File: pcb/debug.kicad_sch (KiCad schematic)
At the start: 2 parts

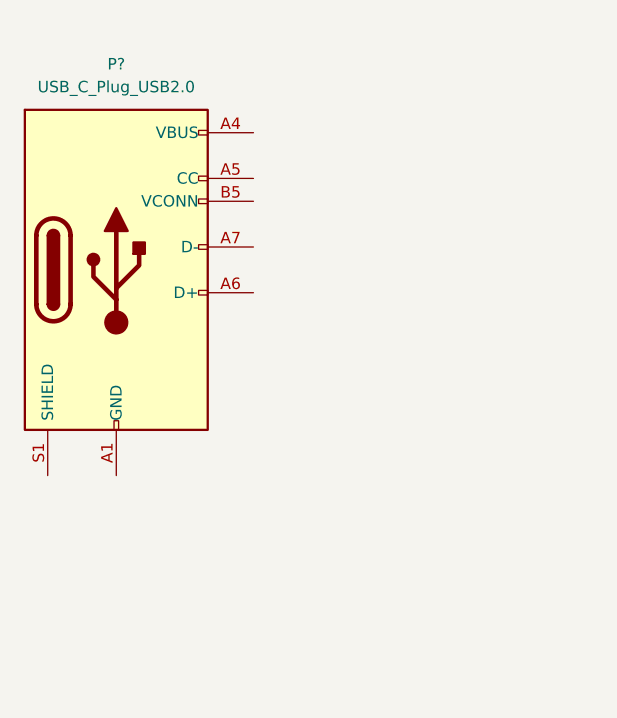
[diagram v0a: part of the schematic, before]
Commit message: add power schematics
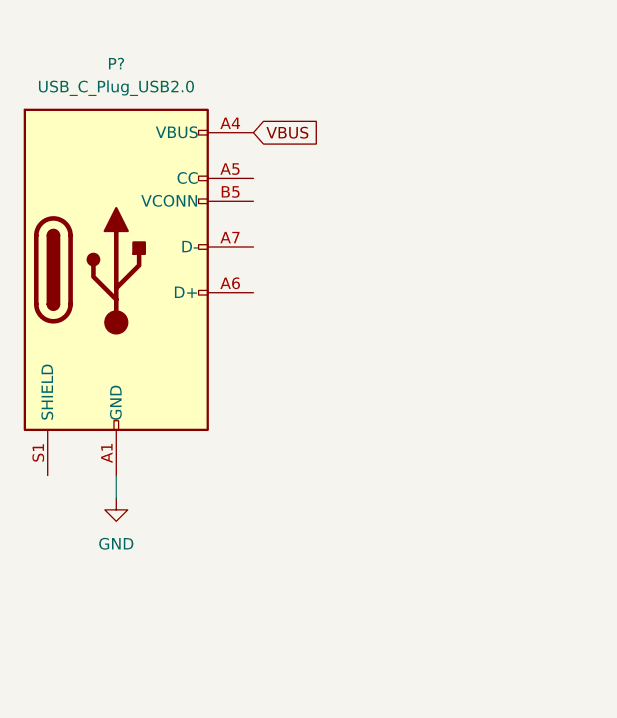
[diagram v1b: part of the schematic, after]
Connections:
- net GND: now reaches P?.A1 (GND), P?.A12 (GND), P?.B1 (GND), P?.B12 (GND)
- net VBUS: now reaches P?.A4 (VBUS), P?.A9 (VBUS), P?.B4 (VBUS), P?.B9 (VBUS)
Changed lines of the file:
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@@
     (title "USB to SPI interface")
+  )
+  (wire (pts (xy 45.72 115.57) (xy 45.72 118.11))
+    (stroke (width 0) (type default) (color 0 0 0 0))
+  )
+  (global_label "VBUS" (shape input) (at 60.96 77.47 0) (fields_autoplaced)
+    (effects (font (size 1.27 1.27)) (justify left))
+    (property "Intersheet References" "${INTERSHEET_REFS}" (id 0) (at 68.2717 77.3906 0)
+      (effects (font (size 1.27 1.27)) (justify left))
+    )
   )
   (symbol (lib_id "Connector:USB_C_Plug_USB2.0") (at 45.72 92.71 0) (unit 1)
@@
     (pin "9")
   )
+  (symbol (lib_id "power:GND") (at 45.72 118.11 0) (unit 1)
+    (in_bom yes) (on_board yes) (fields_autoplaced)
+    (property "Reference" "#PWR?" (id 0) (at 45.72 124.46 0)
+      (effects (font (size 1.27 1.27)) hide)
+    )
+    (property "Value" "GND" (id 1) (at 45.72 123.19 0))
+    (property "Footprint" "" (id 2) (at 45.72 118.11 0)
+      (effects (font (size 1.27 1.27)) hide)
+    )
+    (property "Datasheet" "" (id 3) (at 45.72 118.11 0)
+      (effects (font (size 1.27 1.27)) hide)
+    )
+    (pin "1")
+  )
   (sheet (at 171.45 219.71) (size 24.13 19.05) (fields_autoplaced)
     (stroke (width 0.1524) (type solid) (color 0 0 0 0))
@@
   )
   (symbol_instances
+    (path "/1b1ae3dd-f20e-4dc4-843b-d424ca135075/2e74d807-b0fe-4e20-9ef7-ed84c7863992"
+      (reference "#FLG?") (unit 1) (value "PWR_FLAG") (footprint "")
+    )
+    (path "/1b1ae3dd-f20e-4dc4-843b-d424ca135075/2d21afbd-6859-4669-a772-031efa34f4ca"
+      (reference "#PWR?") (unit 1) (value "+3V3") (footprint "")
+    )
+    (path "/1b1ae3dd-f20e-4dc4-843b-d424ca135075/45f16f4e-0be6-4730-a0ff-76769f804a66"
+      (reference "#PWR?") (unit 1) (value "+5V") (footprint "")
+    )
+    (path "/dfea10a7-1cbe-4c44-a951-08c8c82414b9/50fb4ca1-22a3-4466-ab42-e0b30b8cb45f"
+      (reference "#PWR?") (unit 1) (value "GND") (footprint "")
+    )
+    (path "/dfea10a7-1cbe-4c44-a951-08c8c82414b9/58475425-b42f-4af3-9c27-3bfb381b9dbc"
+      (reference "#PWR?") (unit 1) (value "GND") (footprint "")
+    )
+    (path "/94884f5c-d59b-4b75-abd7-44726b7a235a"
+      (reference "#PWR?") (unit 1) (value "GND") (footprint "")
+    )
+    (path "/1b1ae3dd-f20e-4dc4-843b-d424ca135075/a43f493d-f709-4ca9-9df9-a46685d2f7a2"
+      (reference "#PWR?") (unit 1) (value "GND") (footprint "")
+    )
+    (path "/1b1ae3dd-f20e-4dc4-843b-d424ca135075/bc7f0831-fb41-4e41-b4a1-87de6e384650"
+      (reference "#PWR?") (unit 1) (value "GND") (footprint "")
+    )
+    (path "/1b1ae3dd-f20e-4dc4-843b-d424ca135075/ca0117f5-c935-4a15-9120-d20f94ec645f"
+      (reference "#PWR?") (unit 1) (value "GND") (footprint "")
+    )
+    (path "/1b1ae3dd-f20e-4dc4-843b-d424ca135075/e18d338e-e566-43ef-ab1a-e91845ba4607"
+      (reference "#PWR?") (unit 1) (value "+5V") (footprint "")
+    )
+    (path "/dfea10a7-1cbe-4c44-a951-08c8c82414b9/f0208d8e-9c49-4e8a-9555-afee527cca7a"
+      (reference "#PWR?") (unit 1) (value "GND") (footprint "")
+    )
+    (path "/1b1ae3dd-f20e-4dc4-843b-d424ca135075/f0f17df2-bb70-4da8-ab70-70dc33265364"
+      (reference "#PWR?") (unit 1) (value "GND") (footprint "")
+    )
+    (path "/1b1ae3dd-f20e-4dc4-843b-d424ca135075/f5b12451-8c10-452e-97b4-d0279ae5f0a0"
+      (reference "#PWR?") (unit 1) (value "+5V") (footprint "")
+    )
+    (path "/1b1ae3dd-f20e-4dc4-843b-d424ca135075/9e702b4b-af83-4225-99e7-d3b37033d4f6"
+      (reference "C?") (unit 1) (value "1u") (footprint "")
+    )
+    (path "/1b1ae3dd-f20e-4dc4-843b-d424ca135075/d31985b9-4de6-488d-a2f4-75966192efdf"
+      (reference "C?") (unit 1) (value "1u") (footprint "")
+    )
+    (path "/1b1ae3dd-f20e-4dc4-843b-d424ca135075/fcdaf3af-f4d4-427c-8c20-ed0729a5b02a"
+      (reference "C?") (unit 1) (value "1u") (footprint "")
+    )
+    (path "/1b1ae3dd-f20e-4dc4-843b-d424ca135075/3f6b5f2a-45d9-4080-aba4-0ff576a8a80f"
+      (reference "FB?") (unit 1) (value "600R") (footprint "")
+    )
     (path "/dfea10a7-1cbe-4c44-a951-08c8c82414b9/4ec00cc8-73ee-4a88-8f61-16dd24bb6fe7"
       (reference "J?") (unit 1) (value "09031966921") (footprint "Harting-09031966921-0-0-*")
@@
       (reference "P?") (unit 1) (value "USB_C_Plug_USB2.0") (footprint "")
     )
-    (path "/1b1ae3dd-f20e-4dc4-843b-d424ca135075/64f3e14b-8a0a-445b-842d-7829e058b95b"
-      (reference "Q?") (unit 1) (value "Q_NPN_BCE") (footprint "")
+    (path "/1b1ae3dd-f20e-4dc4-843b-d424ca135075/f8a17ca4-324e-4b9e-940d-3e3a6aba4552"
+      (reference "Q?") (unit 1) (value "Q_PNP_BCE") (footprint "")
+    )
+    (path "/1b1ae3dd-f20e-4dc4-843b-d424ca135075/e6d3f2ec-0651-4501-9d4b-6ed215e299b7"
+      (reference "R?") (unit 1) (value "R_Small") (footprint "")
     )
     (path "/22bb6c80-05a9-4d89-98b0-f4c23fe6c1ce"

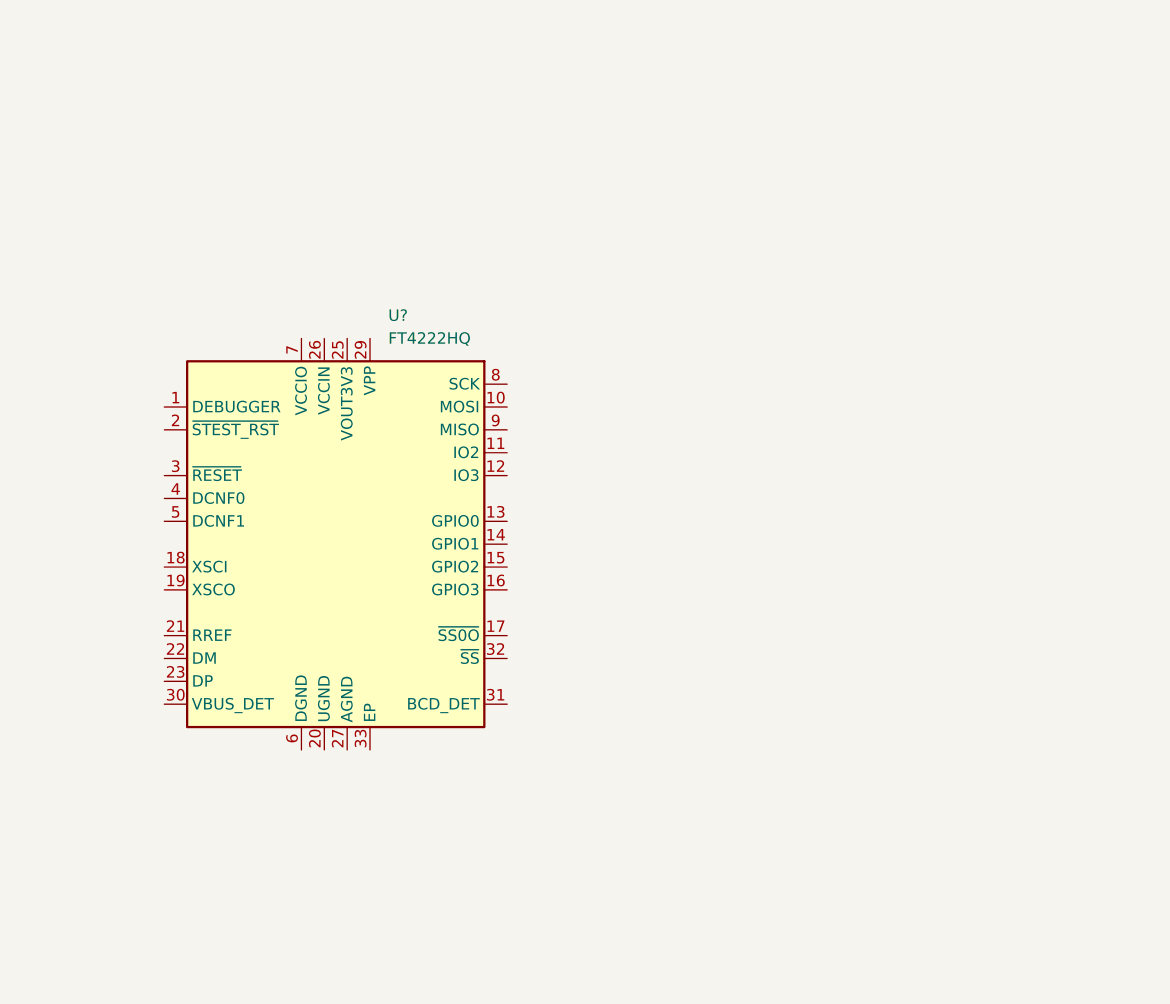
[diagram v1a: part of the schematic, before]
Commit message: start the schematics for the usb to spi interface
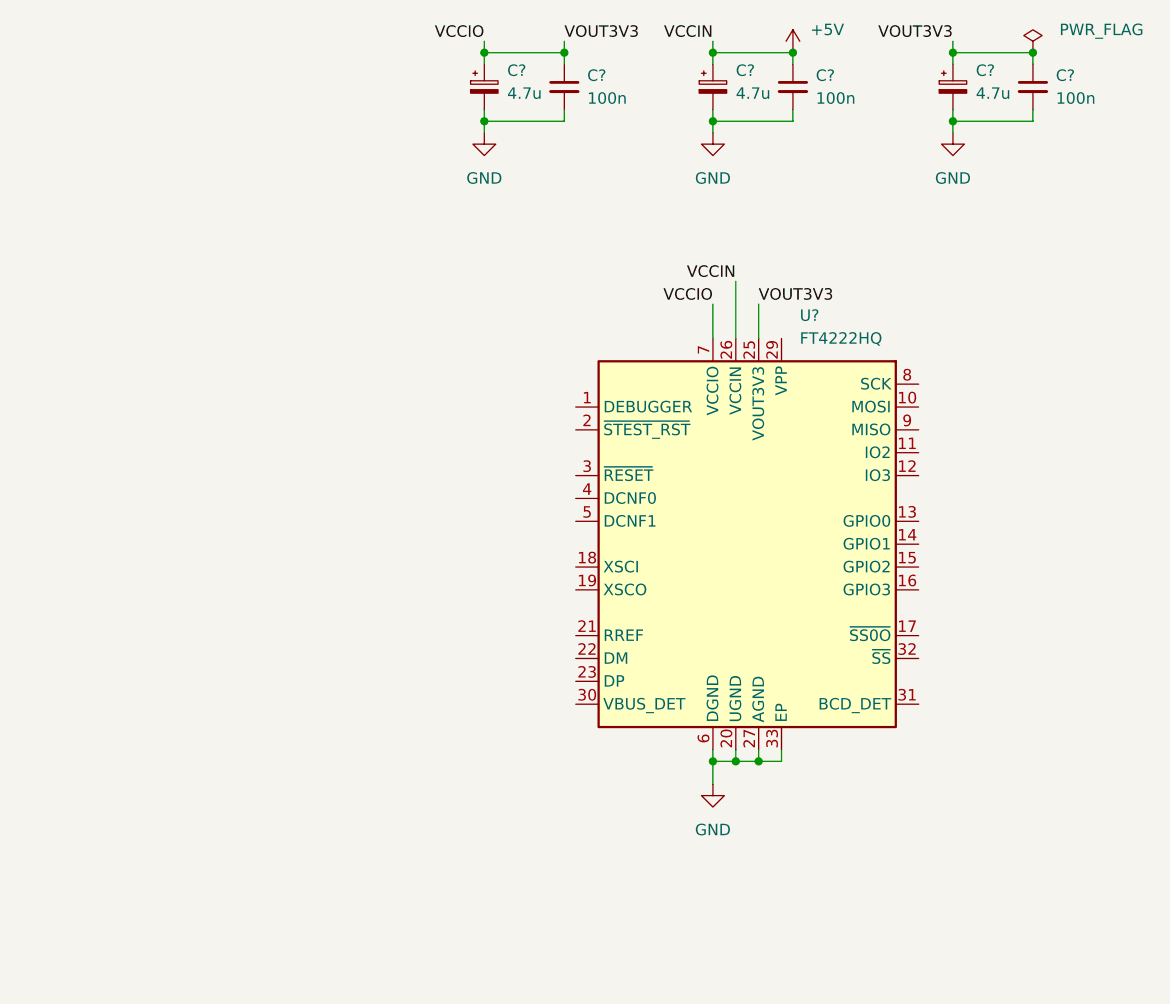
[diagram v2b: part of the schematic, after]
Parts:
- added C? (x3): 4.7u, symbol Device:C_Polarized_Small
- added C? (x3): 100n, symbol Device:C_Small
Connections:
- net GND: now also U?.20 (UGND), U?.24 (UGND), U?.27 (AGND), U?.28 (DGND), U?.33 (EP), U?.6 (DGND), C?.2, C?.2, C?.2, C?.2, C?.2, C?.2
- net VCCIO: now reaches U?.25 (VOUT3V3)
- net VCCIO: now also U?.7 (VCCIO), C?.1, C?.1, C?.1, C?.1
- net +5V: now reaches U?.26 (VCCIN)
- net +5V: now also C?.1, C?.1
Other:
- moved on the sheet: U?
